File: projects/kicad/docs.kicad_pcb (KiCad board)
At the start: 2 copper layers, 90 x 100 mm, 19 parts, among them SW1 SW_PUSH, SW2 SW_PUSH, SW3 SW_PUSH, SW4 SW_PUSH, SW5 SW_PUSH, SW6 SW_PUSH, SW7 RotaryEncoder_Switch, U1 Pico, U3 2.8_240x320_touch_sd_spi

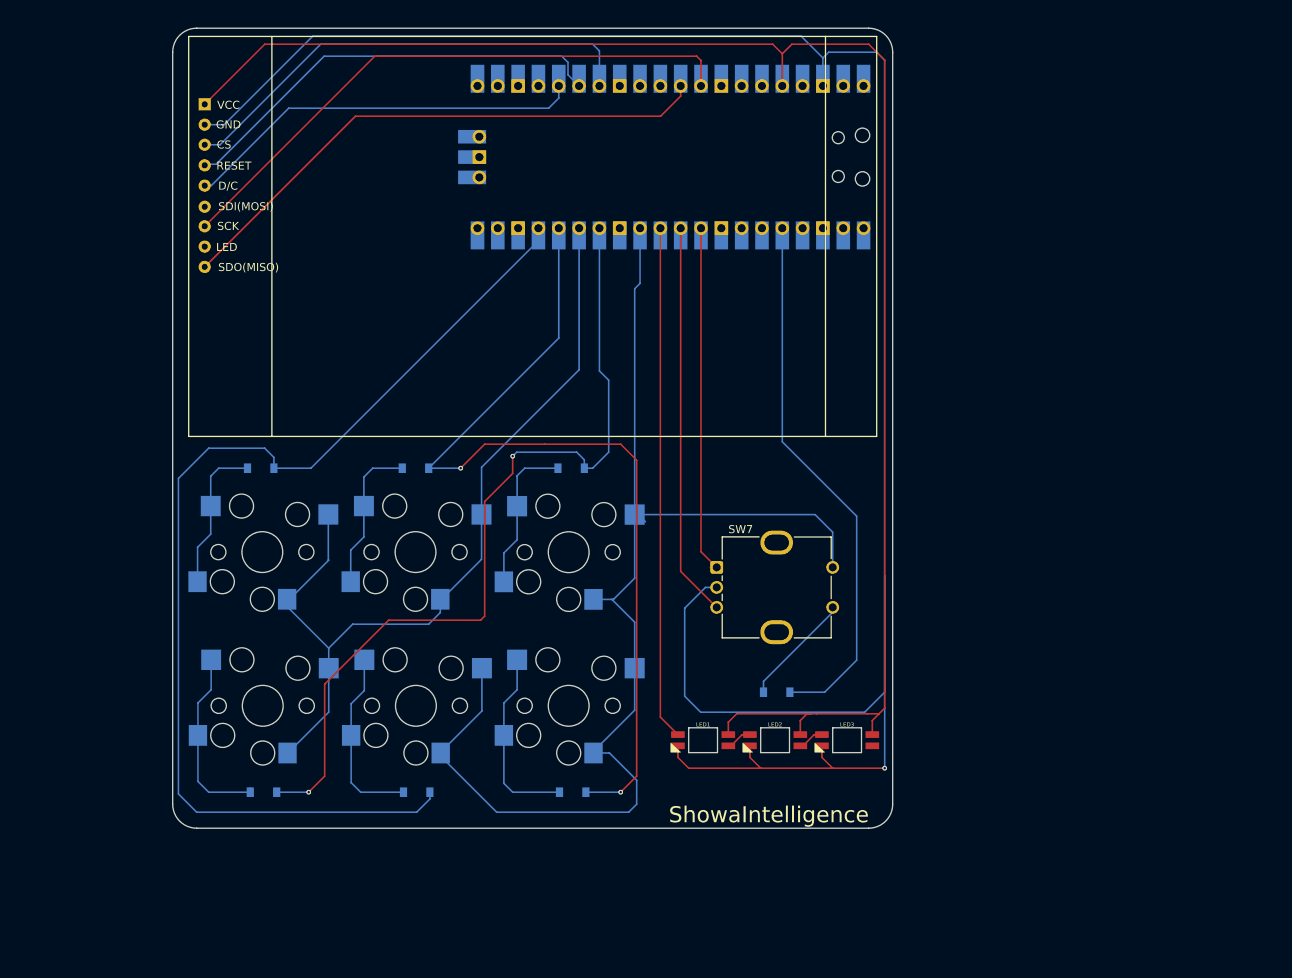
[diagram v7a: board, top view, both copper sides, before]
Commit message: yama_update
・LEDの裏表反転
・基盤固定のためのホールを4つ設置
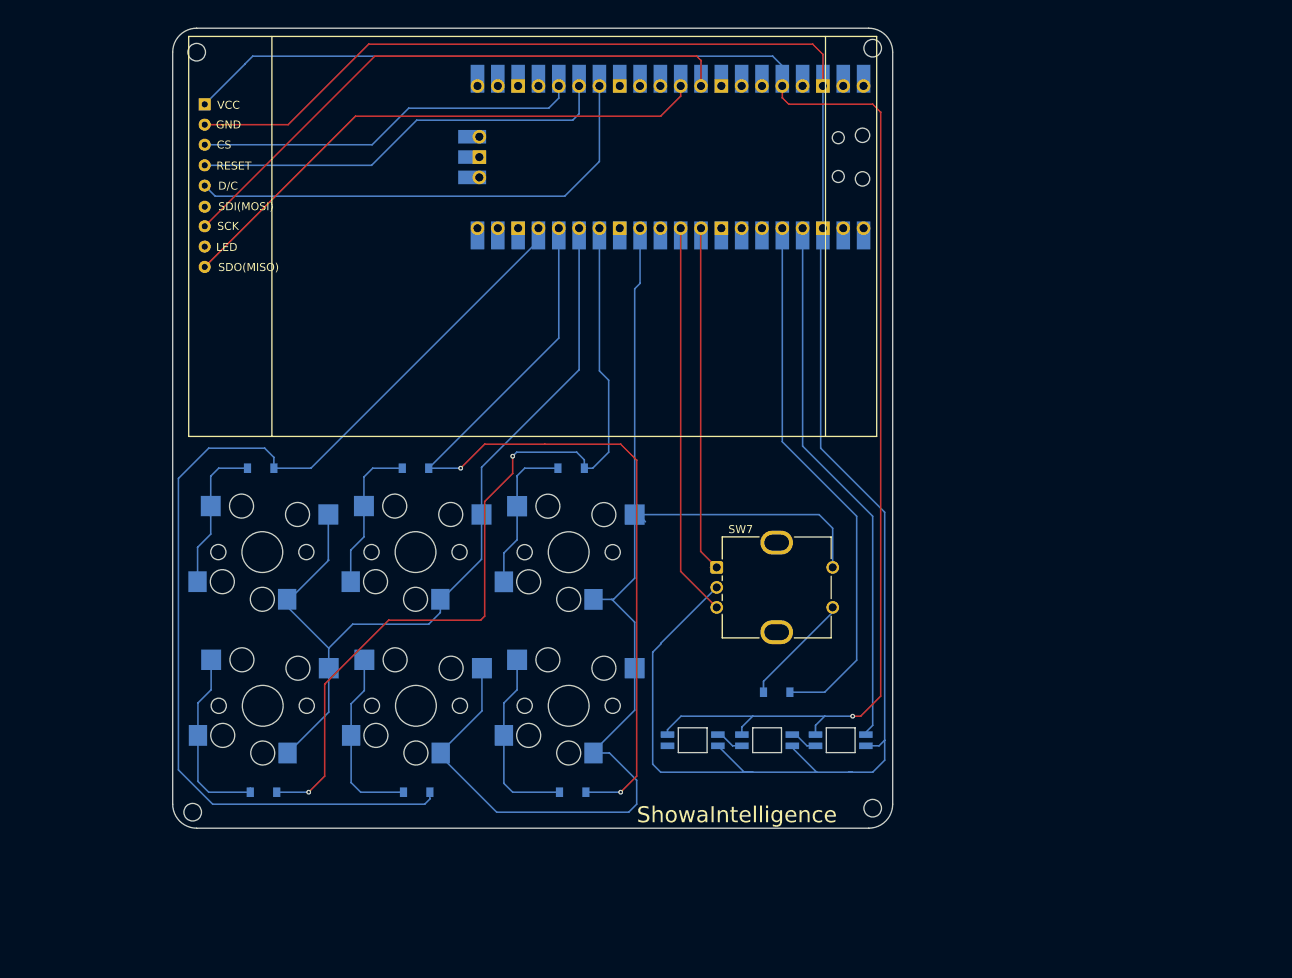
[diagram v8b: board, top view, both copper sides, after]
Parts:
- added Ref**: Val**, kbd_hole:m2_Screw_Hole, F.Cu at (175.5, 25.5)
- added Ref**: Val**, kbd_hole:m2_Screw_Hole, F.Cu at (175.5, 120.5)
- added Ref**: Val**, kbd_hole:m2_Screw_Hole, F.Cu at (90.5, 121.0)
- added Ref**: Val**, kbd_hole:m2_Screw_Hole, F.Cu at (91.0, 26.0)
- LED1, LED2, LED3: moved to B.Cu
- moved LED3 19.3 mm to (153.0, 112.0), turned to 180 degrees
- moved LED1 17.2 mm to (171.5, 112.0), turned to 180 degrees
- moved LED2 1.00 mm to (162.3, 112.0), turned to 180 degrees
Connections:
- U1 pad 11: LED -> unconnected-(U1-GPIO8-Pad11)
- U1 pad 25: DC -> CS
- U1 pad 27: CS -> DC
- U1 pad 3: unconnected-(U1-GND-Pad3) -> GND
- U1 pad 4: unconnected-(U1-GPIO2-Pad4)_1 -> LED
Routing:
- net GND: track 275.8 -> 242.5 mm, vias 1 -> 0
- net CS: track 59.3 -> 48.2 mm
- net DC: track 50.3 -> 61.1 mm
- net 3V3 Out: track 203.6 -> 199.9 mm, vias 0 -> 1
- net LED: track 64.6 -> 67.2 mm
- net Row0: track 135.1 -> 132.5 mm
- net unconnected-(U1-GPIO18-Pad24): track 2.50 -> 0.00 mm
- net RST: track 54.9 -> 52.9 mm
- net Net-(LED1-DOUT): track 4.54 -> 3.48 mm
- net Net-(LED2-DOUT): track 4.12 -> 3.58 mm
